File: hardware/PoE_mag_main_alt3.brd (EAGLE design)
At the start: 149.9 x 124.5 mm, 123 parts, among them IC1 LD1117V33, IC10 PCA9517A, IC11 LD1117V33, IC2 DS1338, IC3 74LVC1T45SOT23-HAND, IC4 ATMEGA1284, IC5 MCP2200, IC6 TSR 1-2450, IC7 74LVC1T45SOT23-HAND, IC8 74LVC1T45SOT23-HAND, IC9 74LVC1T45SOT23-HAND, Q1 BSS138, Q3 BUK98150-55A, X1 PWR, X2 JTAG, X3 USB, X4 CONN-SMATHD, X5 UFL, X6 MICRO-SD-SOCKETHIROSE-DM3D, X7 RJ45, X8 RJ11, X9 22-23-2021, Y1 32k768, Y2 16MHz, Y3 12MHz

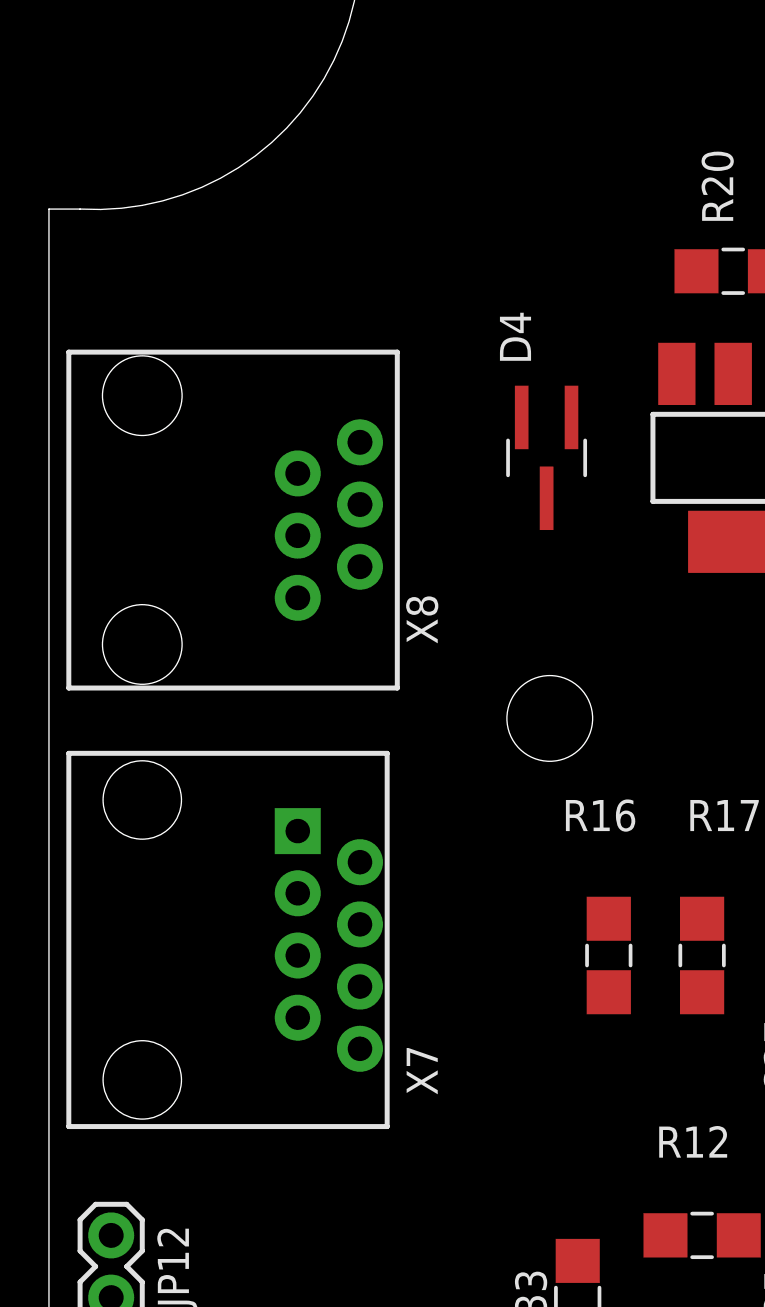
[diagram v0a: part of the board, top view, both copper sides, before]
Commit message: Add Powerpax reg option, move RJ11/45 connectors
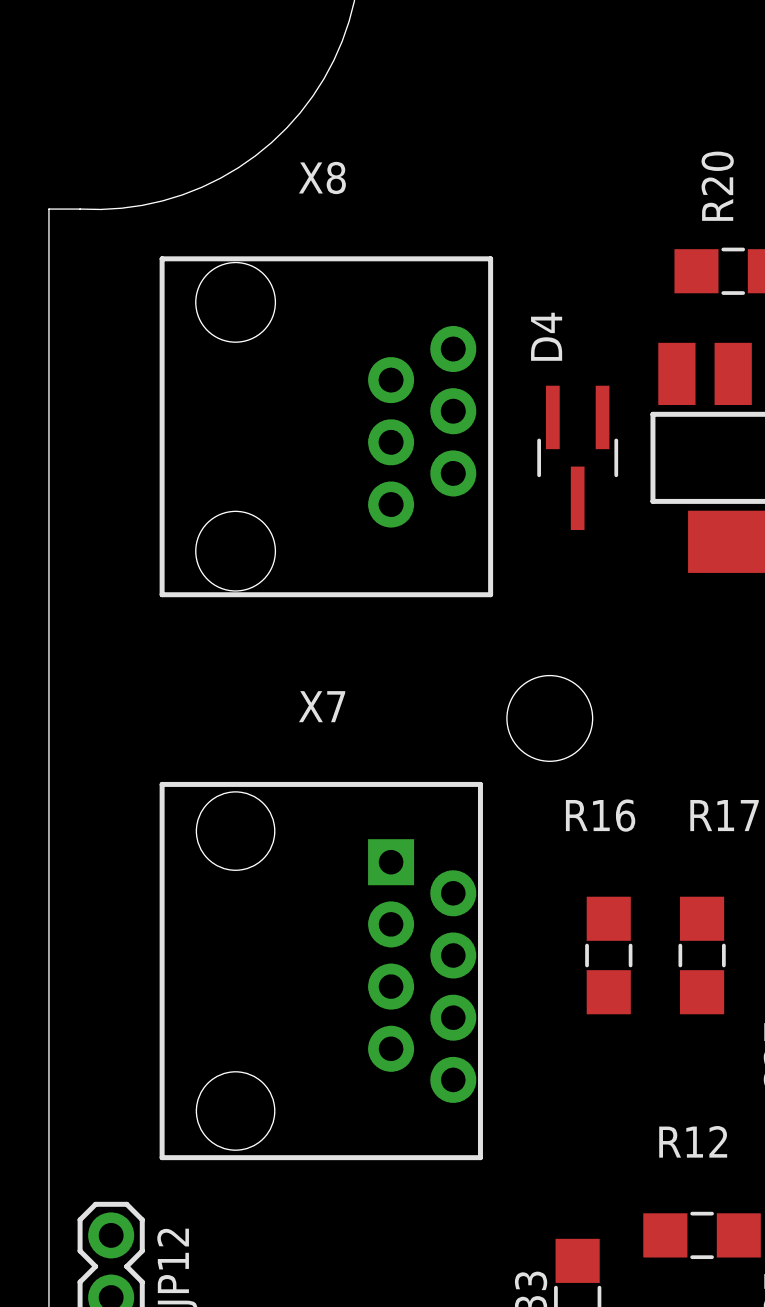
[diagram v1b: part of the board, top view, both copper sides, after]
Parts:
- moved X8 5.39 mm to (7.62, 96.5)
- moved X7 4.02 mm to (7.62, 69.2)
- moved D4 1.27 mm to (21.6, 90.2)
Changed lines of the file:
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@@
 <attribute name="NAME" x="40.64" y="46.355" size="1.27" layer="25" ratio="10" rot="R90"/>
 </element>
-<element name="X7" library="SteveMarple" package="RJ45-8" value="RJ45" x="3.81" y="70.485" smashed="yes" rot="R270">
-<attribute name="NAME" x="15.875" y="64.135" size="1.27" layer="25" ratio="10" rot="R90"/>
-<attribute name="VALUE" x="17.78" y="64.135" size="1.27" layer="27" ratio="10" rot="R90"/>
+<element name="X7" library="SteveMarple" package="RJ45-8" value="RJ45" x="7.62" y="69.215" smashed="yes" rot="R270">
+<attribute name="NAME" x="10.16" y="79.375" size="1.27" layer="25" ratio="10"/>
+<attribute name="VALUE" x="10.16" y="77.47" size="1.27" layer="27" ratio="10"/>
 </element>
 <element name="JP12" library="SparkFun" package="1X02" value="5V LINK" x="2.54" y="55.88" smashed="yes" rot="R90">
@@
 <attribute name="VALUE" x="7.62" y="57.15" size="1.27" layer="27" ratio="10" rot="R90" align="bottom-center"/>
 </element>
-<element name="X8" library="SteveMarple" package="RJ11-6" value="RJ11" x="3.81" y="92.71" smashed="yes" rot="R270">
-<attribute name="NAME" x="15.875" y="82.55" size="1.27" layer="25" ratio="10" rot="R90"/>
-<attribute name="VALUE" x="17.78" y="82.55" size="1.27" layer="27" ratio="10" rot="R90"/>
+<element name="X8" library="SteveMarple" package="RJ11-6" value="RJ11" x="7.62" y="96.52" smashed="yes" rot="R270">
+<attribute name="NAME" x="10.16" y="100.965" size="1.27" layer="25" ratio="10"/>
+<attribute name="VALUE" x="10.16" y="99.06" size="1.27" layer="27" ratio="10"/>
 </element>
 <element name="JP13" library="SparkFun" package="1X03" value="MAG VCC" x="2.54" y="50.8" smashed="yes" rot="R270">
@@
 <attribute name="VALUE" x="55.245" y="83.82" size="1.27" layer="27" ratio="10"/>
 </element>
-<element name="D4" library="SteveMarple" package="SOT23-3-HAND" value="BAS21" x="20.32" y="90.17" smashed="yes" rot="R270">
-<attribute name="NAME" x="19.685" y="93.98" size="1.27" layer="25" ratio="10" rot="SR90"/>
-<attribute name="VALUE" x="21.59" y="93.98" size="1.27" layer="27" ratio="10" rot="SR90"/>
+<element name="D4" library="SteveMarple" package="SOT23-3-HAND" value="BAS21" x="21.59" y="90.17" smashed="yes" rot="R270">
+<attribute name="NAME" x="20.955" y="93.98" size="1.27" layer="25" ratio="10" rot="SR90"/>
+<attribute name="VALUE" x="22.86" y="93.98" size="1.27" layer="27" ratio="10" rot="SR90"/>
 </element>
 <element name="X9" library="con-molex" package="22-23-2021" value="22-23-2021" x="36.83" y="96.52" smashed="yes" rot="R180">
@@
 <wire x1="63.754" y1="91.821" x2="75.52" y2="87.63" width="0" layer="19" extent="1-1"/>
 <wire x1="63.271" y1="95.25" x2="63.754" y2="91.821" width="0" layer="19" extent="1-1"/>
-<wire x1="12.7" y1="71.12" x2="21.59" y2="57.379" width="0" layer="19" extent="1-1"/>
-<wire x1="10.16" y1="72.39" x2="12.7" y2="71.12" width="0" layer="19" extent="1-1"/>
-<wire x1="12.7" y1="88.265" x2="10.16" y2="72.39" width="0" layer="19" extent="1-1"/>
-<wire x1="10.16" y1="89.535" x2="12.7" y2="88.265" width="0" layer="19" extent="1-1"/>
-<wire x1="21.336" y1="91.821" x2="12.7" y2="88.265" width="0" layer="19" extent="1-1"/>
-<wire x1="25.64" y1="93.5994" x2="21.336" y2="91.821" width="0" layer="19" extent="1-1"/>
+<wire x1="16.51" y1="69.85" x2="21.59" y2="57.379" width="0" layer="19" extent="1-1"/>
+<wire x1="13.97" y1="71.12" x2="16.51" y2="69.85" width="0" layer="19" extent="1-1"/>
+<wire x1="16.51" y1="92.075" x2="13.97" y2="71.12" width="0" layer="19" extent="1-1"/>
+<wire x1="13.97" y1="93.345" x2="16.51" y2="92.075" width="0" layer="19" extent="1-1"/>
+<wire x1="22.606" y1="91.821" x2="16.51" y2="92.075" width="0" layer="19" extent="1-1"/>
+<wire x1="25.64" y1="93.5994" x2="22.606" y2="91.821" width="0" layer="19" extent="1-1"/>
 <wire x1="26.441" y1="97.79" x2="25.64" y2="93.5994" width="0" layer="19" extent="1-1"/>
 <wire x1="45.72" y1="96.52" x2="63.271" y2="95.25" width="0" layer="19" extent="1-1"/>
@@
 <wire x1="121.691" y1="21.59" x2="99.06" y2="38.1" width="0" layer="19" extent="1-1"/>
 <wire x1="38.1" y1="96.52" x2="99.06" y2="45.72" width="0" layer="19" extent="1-1"/>
-<wire x1="12.7" y1="90.805" x2="38.1" y2="96.52" width="0" layer="19" extent="1-1"/>
-<wire x1="12.7" y1="73.66" x2="12.7" y2="90.805" width="0" layer="19" extent="1-1"/>
-<wire x1="2.54" y1="50.8" x2="12.7" y2="73.66" width="0" layer="19" extent="1-1"/>
+<wire x1="16.51" y1="94.615" x2="38.1" y2="96.52" width="0" layer="19" extent="1-1"/>
+<wire x1="16.51" y1="72.39" x2="16.51" y2="94.615" width="0" layer="19" extent="1-1"/>
+<wire x1="2.54" y1="50.8" x2="16.51" y2="72.39" width="0" layer="19" extent="1-1"/>
 </signal>
 <signal name="AVCC" class="1">
@@
 <wire x1="26.67" y1="68.351" x2="31.75" y2="67.539" width="0" layer="19" extent="1-1"/>
 <wire x1="22.86" y1="68.351" x2="26.67" y2="68.351" width="0" layer="19" extent="1-1"/>
-<wire x1="12.7" y1="68.58" x2="22.86" y2="68.351" width="0" layer="19" extent="1-1"/>
-<wire x1="2.54" y1="58.42" x2="12.7" y2="68.58" width="0" layer="19" extent="1-1"/>
-<wire x1="12.7" y1="85.725" x2="12.7" y2="68.58" width="0" layer="19" extent="1-1"/>
+<wire x1="16.51" y1="67.31" x2="22.86" y2="68.351" width="0" layer="19" extent="1-1"/>
+<wire x1="2.54" y1="58.42" x2="16.51" y2="67.31" width="0" layer="19" extent="1-1"/>
+<wire x1="16.51" y1="89.535" x2="16.51" y2="67.31" width="0" layer="19" extent="1-1"/>
 </signal>
 <signal name="MAG_SCL">
@@
 <contactref element="R17" pad="1"/>
 <wire x1="26.67" y1="71.349" x2="31.6738" y2="71.755" width="0" layer="19" extent="1-1"/>
-<wire x1="10.16" y1="69.85" x2="26.67" y2="71.349" width="0" layer="19" extent="1-1"/>
-<wire x1="10.16" y1="86.995" x2="10.16" y2="69.85" width="0" layer="19" extent="1-1"/>
+<wire x1="13.97" y1="68.58" x2="26.67" y2="71.349" width="0" layer="19" extent="1-1"/>
+<wire x1="13.97" y1="90.805" x2="13.97" y2="68.58" width="0" layer="19" extent="1-1"/>
 </signal>
 <signal name="MAG_SDA">
@@
 <contactref element="R16" pad="1"/>
 <wire x1="22.86" y1="71.349" x2="31.6738" y2="73.025" width="0" layer="19" extent="1-1"/>
-<wire x1="10.16" y1="67.31" x2="22.86" y2="71.349" width="0" layer="19" extent="1-1"/>
-<wire x1="10.16" y1="84.455" x2="10.16" y2="67.31" width="0" layer="19" extent="1-1"/>
+<wire x1="13.97" y1="66.04" x2="22.86" y2="71.349" width="0" layer="19" extent="1-1"/>
+<wire x1="13.97" y1="88.265" x2="13.97" y2="66.04" width="0" layer="19" extent="1-1"/>
 </signal>
 <signal name="N$26" class="1">
 <contactref element="X7" pad="8"/>
 <contactref element="JP13" pad="2"/>
-<wire x1="2.54" y1="48.26" x2="12.7" y2="66.04" width="0" layer="19" extent="1-1"/>
+<wire x1="2.54" y1="48.26" x2="16.51" y2="64.77" width="0" layer="19" extent="1-1"/>
 </signal>
 <signal name="FAN_CTRL">
@@
 <wire x1="27.94" y1="93.5994" x2="35.56" y2="96.52" width="0" layer="19" extent="1-1"/>
 <wire x1="27.94" y1="86.7406" x2="27.94" y2="93.5994" width="0" layer="19" extent="1-1"/>
-<wire x1="20.32" y1="88.519" x2="27.94" y2="86.7406" width="0" layer="19" extent="1-1"/>
+<wire x1="21.59" y1="88.519" x2="27.94" y2="86.7406" width="0" layer="19" extent="1-1"/>
 </signal>
 <signal name="N$29">

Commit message: Minor changes
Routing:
- net GND: track 209.1 -> 1089.1 mm, vias 27 -> 33
- net VCC: track 40.5 -> 468.5 mm, vias 0 -> 12
- net +3V3: track 37.8 -> 344.7 mm, vias 0 -> 6
- net 20(SDA): track 0.00 -> 262.0 mm, vias 0 -> 1
- net VIN: track 0.00 -> 260.8 mm, vias 0 -> 1
- net 1(TX0): track 0.00 -> 220.3 mm, vias 0 -> 2
- net 21(SCL): track 0.00 -> 217.6 mm, vias 0 -> 2
- net !RESET: track 0.00 -> 188.9 mm, vias 0 -> 4
- net +5V: track 0.00 -> 159.1 mm
- net 2(RX1): track 0.00 -> 142.6 mm, vias 0 -> 3
- net 0(RX0): track 0.00 -> 141.3 mm, vias 0 -> 3
- net 3(TX1): track 0.00 -> 138.1 mm, vias 0 -> 2
- net 13(SCK): track 0.00 -> 115.2 mm, vias 0 -> 4
- net 22: track 0.00 -> 112.6 mm, vias 0 -> 1
- net VBATT: track 0.00 -> 112.4 mm, vias 0 -> 2
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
